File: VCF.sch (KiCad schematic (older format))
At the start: 70 parts, among them J101 AudioJack2, J102 AudioJack2, J103 AudioJack2, J104 AudioJack2, J105 Conn_02x05_Odd_Even, J106 AudioJack2, Q101 2N3906, Q102 2N3906, Q103 Q_NJFET_DSG, U101 TL072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

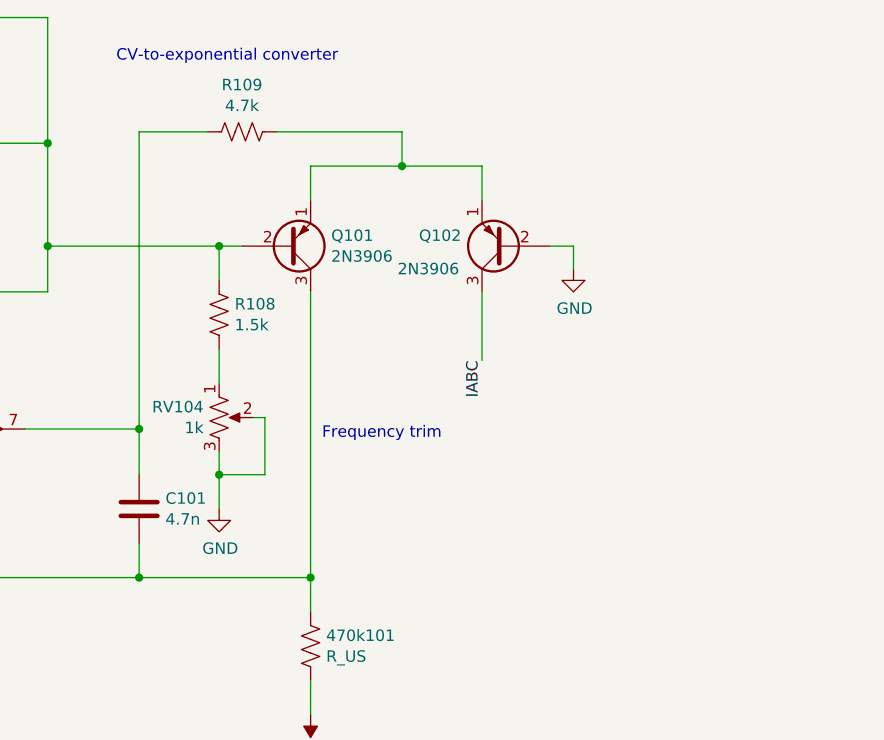
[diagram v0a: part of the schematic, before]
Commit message: Added SMT option for PNP current mirror
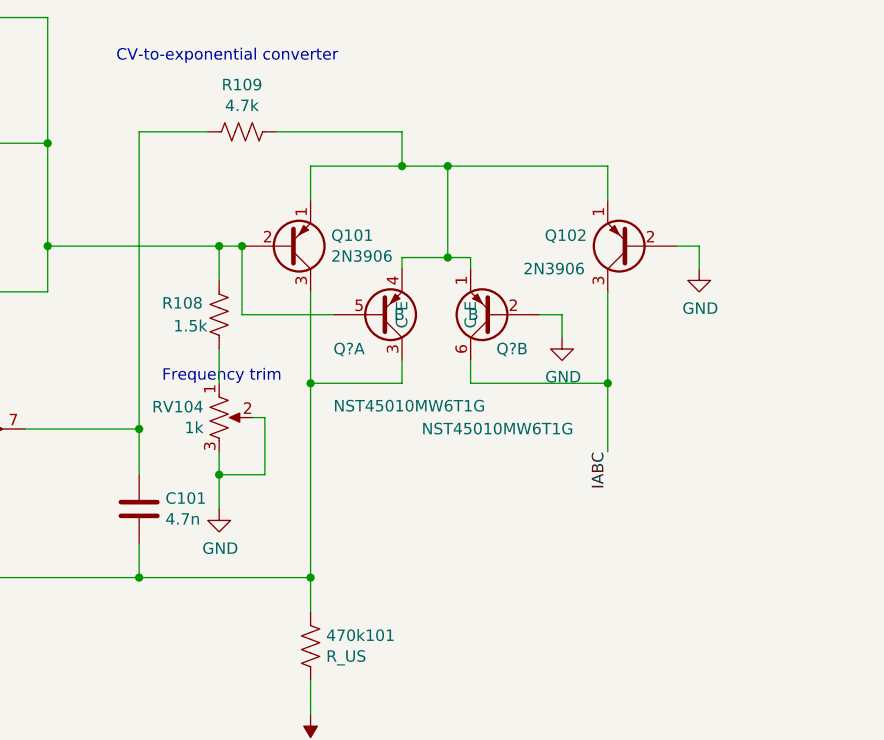
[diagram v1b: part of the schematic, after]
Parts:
- added Q? (x2): NST45010MW6T1G, symbol NST45010MW6T1G:NST45010MW6T1G
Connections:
- net GND: now also Q?.2 (B)
- net IABC: now also Q?.6 (C)
- net at 470k101.1, C101.2, Q101.3 (C)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: now also Q?.3 (C)
- net at Q101.2 (B), R101.1, R102.1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: now also Q?.5 (B)
- net at Q101.1 (E), Q102.1 (E), R109.1: now also Q?.1 (E), Q?.4 (E)
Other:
- moved on the sheet: Q102
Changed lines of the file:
@@
 U 1 1 60ABB8F0
 P 2900 5750
-F 0 "R108" H 2968 5796 50  0000 L CNN
-F 1 "1.5k" H 2968 5705 50  0000 L CNN
+F 0 "R108" H 2650 5800 50  0000 L CNN
+F 1 "1.5k" H 2700 5700 50  0000 L CNN
 F 2 "" V 2940 5740 50  0001 C CNN
 F 3 "~" H 2900 5750 50  0001 C CNN
@@
 	3300 5100 3700 5100
 Wire Wire Line
-	4050 5100 4050 5250
+	4600 5100 4600 5250
 Wire Wire Line
 	3150 4950 3700 4950
 Wire Wire Line
 	3700 4950 3700 5100
-Connection ~ 3700 5100
-Wire Wire Line
-	3700 5100 4050 5100
 Wire Wire Line
 	2550 4950 2550 6250
@@
 	2150 5450 2150 5650
 Wire Wire Line
-	4450 5550 4450 5450
-Wire Wire Line
-	4450 5450 4350 5450
+	5000 5550 5000 5450
+Wire Wire Line
+	5000 5450 4900 5450
 $Comp
 L power:GND #PWR0114
 U 1 1 60CA0F0A
-P 4450 5550
-F 0 "#PWR0114" H 4450 5300 50  0001 C CNN
-F 1 "GND" H 4455 5377 50  0000 C CNN
-F 2 "" H 4450 5550 50  0001 C CNN
-F 3 "" H 4450 5550 50  0001 C CNN
-	1    4450 5550
-	1    0    0    -1
-$EndComp
-Wire Wire Line
-	4050 5950 4050 5650
-Text Label 4050 5950 3    50   ~ 0
+P 5000 5550
+F 0 "#PWR0114" H 5000 5300 50  0001 C CNN
+F 1 "GND" H 5005 5377 50  0000 C CNN
+F 2 "" H 5000 5550 50  0001 C CNN
+F 3 "" H 5000 5550 50  0001 C CNN
+	1    5000 5550
+	1    0    0    -1
+$EndComp
+Text Label 4600 6350 3    50   ~ 0
 IABC
 $Comp
@@
 	1150 5900 1150 5800
 Wire Wire Line
-	3300 5650 3300 6900
+	3300 5650 3300 6050
 Wire Wire Line
 	2550 6900 3300 6900
@@
 Text Notes 9650 5150 0    50   ~ 0
 Power connector and decoupling
-Text Notes 3350 6300 0    50   ~ 0
+Text Notes 2650 6050 0    50   ~ 0
 Frequency trim
 $Comp
 L Transistor_BJT:2N3906 Q102
 U 1 1 61358B0B
-P 4150 5450
-F 0 "Q102" H 4341 5404 50  0000 L CNN
-F 1 "2N3906" H 4350 5550 50  0000 L CNN
-F 2 "Package_TO_SOT_THT:TO-92_Inline" H 4350 5375 50  0001 L CIN
-F 3 "https://www.onsemi.com/pub/Collateral/2N3906-D.PDF" H 4150 5450 50  0001 L CNN
-	1    4150 5450
+P 4700 5450
+F 0 "Q102" H 4891 5404 50  0000 L CNN
+F 1 "2N3906" H 4900 5550 50  0000 L CNN
+F 2 "Package_TO_SOT_THT:TO-92_Inline" H 4900 5375 50  0001 L CIN
+F 3 "https://www.onsemi.com/pub/Collateral/2N3906-D.PDF" H 4700 5450 50  0001 L CNN
+	1    4700 5450
 	-1   0    0    1
 $EndComp
@@
 NoConn ~ 6650 7450
 NoConn ~ 6250 7350
+$Comp
+L NST45010MW6T1G:NST45010MW6T1G Q?
+U 1 1 60A552FA
+P 3700 5250
+F 0 "Q?" H 3400 5900 50  0000 L CNN
+F 1 "NST45010MW6T1G" H 3400 6150 50  0000 L CNN
+F 2 "" H 3700 5250 50  0001 C CNN
+F 3 "" H 3700 5250 50  0001 C CNN
+	1    3700 5250
+	1    0    0    1
+$EndComp
+$Comp
+L NST45010MW6T1G:NST45010MW6T1G Q?
+U 2 1 60A57316
+P 4000 5250
+F 0 "Q?" H 3750 5900 50  0000 L CNN
+F 1 "NST45010MW6T1G" H 3550 6250 50  0000 L CNN
+F 2 "" H 4000 5250 50  0001 C CNN
+F 3 "" H 4000 5250 50  0001 C CNN
+	2    4000 5250
+	-1   0    0    1
+$EndComp
+Wire Wire Line
+	3700 5950 3700 6050
+Wire Wire Line
+	3700 6050 3300 6050
+Connection ~ 3300 6050
+Wire Wire Line
+	3300 6050 3300 6900
+Wire Wire Line
+	3700 5100 3900 5100
+Connection ~ 3700 5100
+Wire Wire Line
+	3700 5500 3700 5550
+Wire Wire Line
+	4000 5550 4000 5500
+Wire Wire Line
+	3700 5500 3900 5500
+Wire Wire Line
+	3900 5500 3900 5100
+Connection ~ 3900 5500
+Wire Wire Line
+	3900 5500 4000 5500
+Connection ~ 3900 5100
+Wire Wire Line
+	3900 5100 4600 5100
+Wire Wire Line
+	4600 6050 4000 6050
+Wire Wire Line
+	4000 6050 4000 5950
+Wire Wire Line
+	4600 5650 4600 6050
+Wire Wire Line
+	4600 6350 4600 6050
+Connection ~ 4600 6050
+Wire Wire Line
+	4400 5850 4400 5750
+Wire Wire Line
+	4400 5750 4300 5750
+$Comp
+L power:GND #PWR?
+U 1 1 60B3557E
+P 4400 5850
+F 0 "#PWR?" H 4400 5600 50  0001 C CNN
+F 1 "GND" H 4405 5677 50  0000 C CNN
+F 2 "" H 4400 5850 50  0001 C CNN
+F 3 "" H 4400 5850 50  0001 C CNN
+	1    4400 5850
+	1    0    0    -1
+$EndComp
+Wire Wire Line
+	3400 5750 3000 5750
+Wire Wire Line
+	3000 5750 3000 5450
+Connection ~ 3000 5450
 $EndSCHEMATC

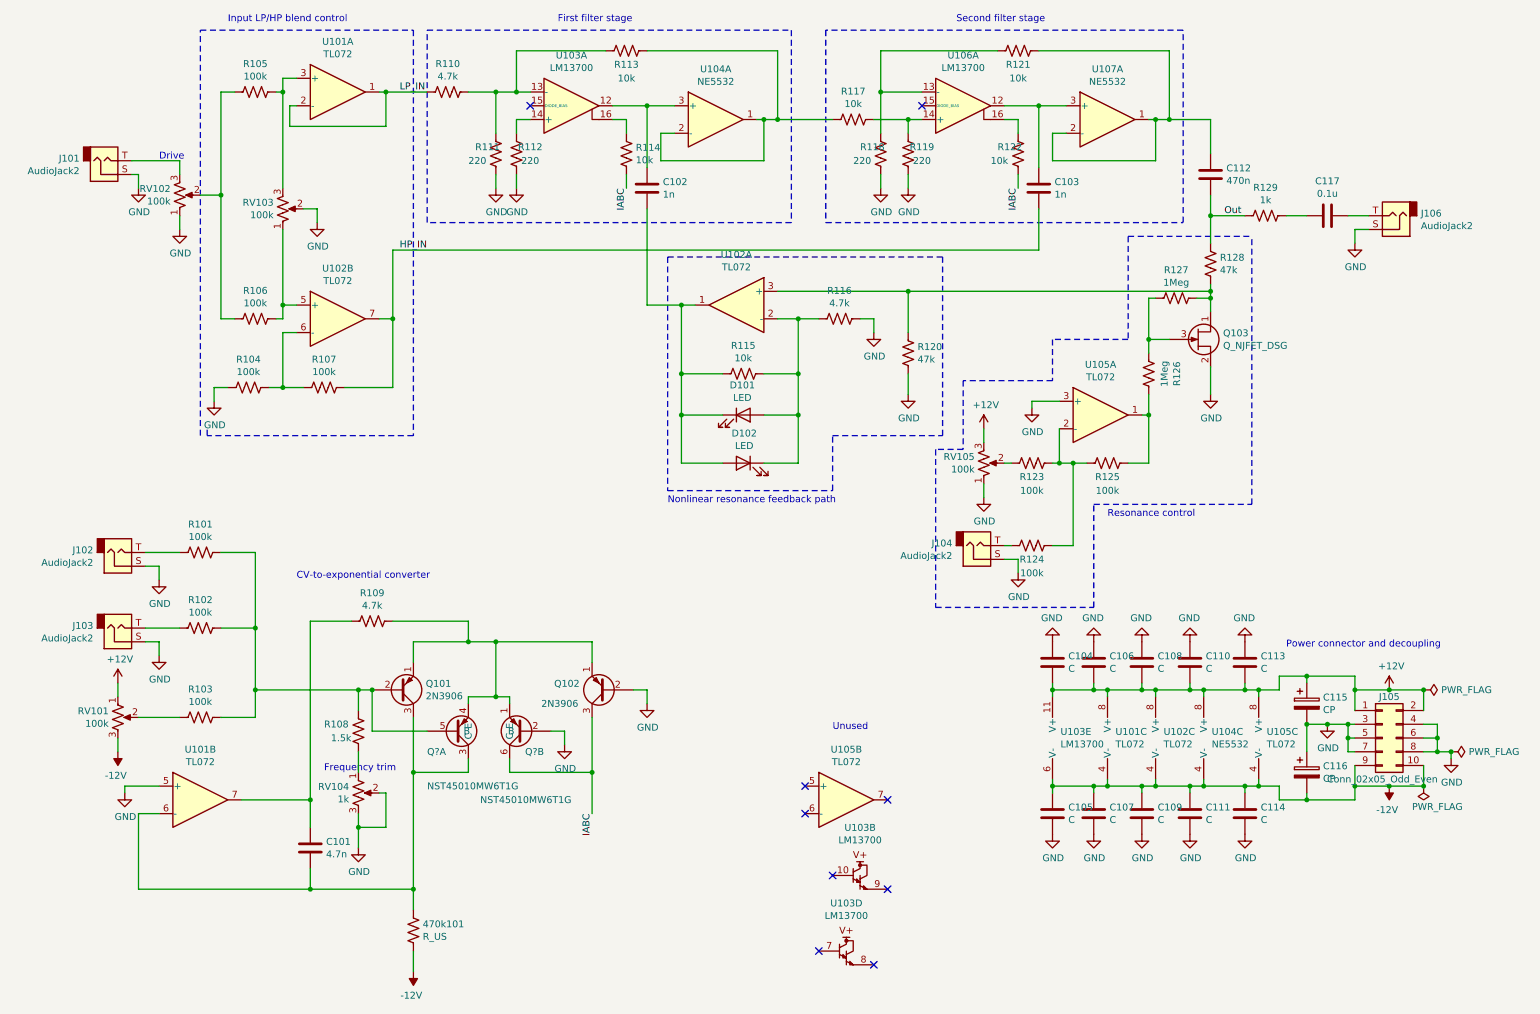
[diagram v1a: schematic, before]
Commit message: Assigned footprints to all components
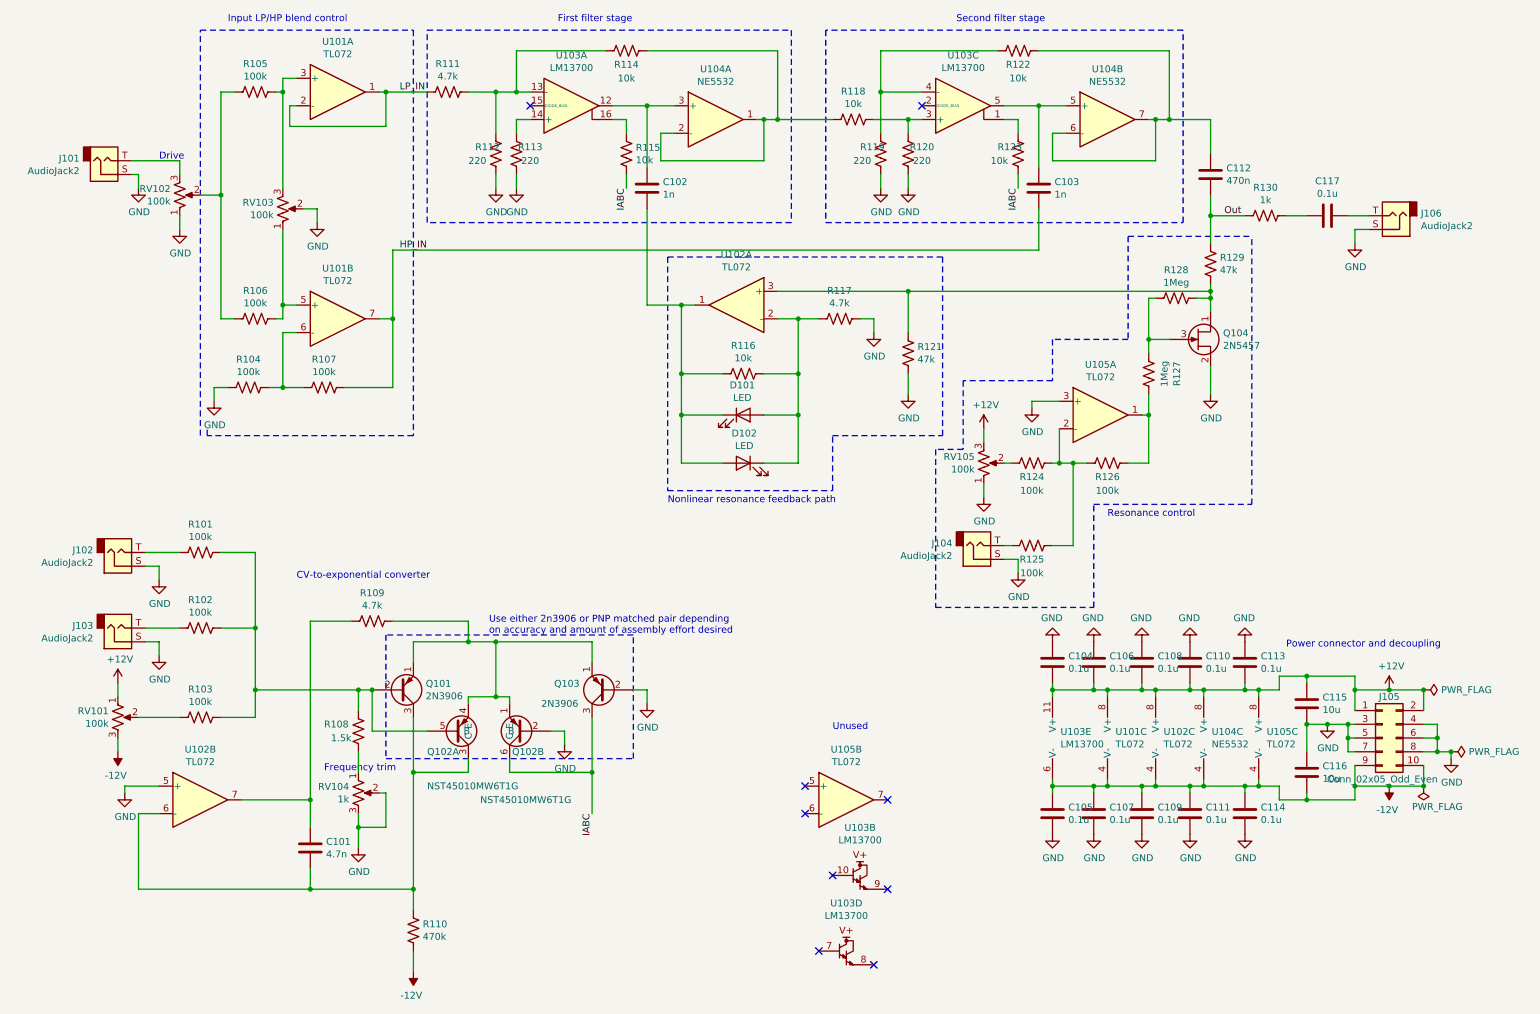
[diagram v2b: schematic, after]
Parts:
- removed C115, C116: CP, symbol Device:CP
- added C115, C116: 10u, Capacitor_SMD:C_0402_1005Metric, symbol Device:C
- C101: footprint (none) -> Capacitor_SMD:C_0402_1005Metric; LCSC (none) -> C1538
- C102, C103: footprint (none) -> Capacitor_SMD:C_0402_1005Metric; LCSC (none) -> C1523
- C104, C105, C106, C107, C108, C109, C110, C111, C113, C114: value C -> 0.1u; footprint (none) -> Capacitor_SMD:C_0402_1005Metric; LCSC (none) -> C1525
- C112: footprint (none) -> Capacitor_SMD:C_0402_1005Metric; LCSC (none) -> C47339
- C117: footprint (none) -> Capacitor_SMD:C_0402_1005Metric; LCSC (none) -> C1525
- D101, D102: footprint (none) -> LED_THT:LED_D5.0mm
- J101, J102, J103, J104, J106: footprint (none) -> A-5513:A-5513
- J105: footprint (none) -> Connector_PinHeader_2.54mm:PinHeader_2x05_P2.54mm_Vertical
- Q102: renamed from Q?; footprint (none) -> Package_TO_SOT_SMD:SOT-363_SC-70-6_Handsoldering
- Q104: renamed from Q103; value Q_NJFET_DSG -> 2N5457; footprint (none) -> Package_TO_SOT_THT:TO-92_Inline
- R101, R102, R103, R104, R105, R106, R107: footprint (none) -> Resistor_SMD:R_0402_1005Metric; LCSC (none) -> C25741
- R108: footprint (none) -> Resistor_SMD:R_0402_1005Metric; LCSC (none) -> C25867
- R109: footprint (none) -> Resistor_SMD:R_0402_1005Metric; LCSC (none) -> C25900
- R110: renamed from 470k101; value R_US -> 470k; footprint (none) -> Resistor_SMD:R_0402_1005Metric; LCSC (none) -> C25792
- R111: renamed from R110; footprint (none) -> Resistor_SMD:R_0402_1005Metric; LCSC (none) -> C25900
- R112: renamed from R111; footprint (none) -> Resistor_SMD:R_0402_1005Metric; LCSC (none) -> C25091
- R113: renamed from R112; footprint (none) -> Resistor_SMD:R_0402_1005Metric; LCSC (none) -> C25091
- R114: renamed from R113; footprint (none) -> Resistor_SMD:R_0402_1005Metric; LCSC (none) -> C25744
- R115: renamed from R114; footprint (none) -> Resistor_SMD:R_0402_1005Metric; LCSC (none) -> C25744
- R116: renamed from R115; footprint (none) -> Resistor_SMD:R_0402_1005Metric; LCSC (none) -> C25744
- R117: renamed from R116; footprint (none) -> Resistor_SMD:R_0402_1005Metric; LCSC (none) -> C25900
- R118: renamed from R117; footprint (none) -> Resistor_SMD:R_0402_1005Metric; LCSC (none) -> C25744
- R119: renamed from R118; footprint (none) -> Resistor_SMD:R_0402_1005Metric; LCSC (none) -> C25091
- R120: renamed from R119; footprint (none) -> Resistor_SMD:R_0402_1005Metric; LCSC (none) -> C25091
- R121: renamed from R120; footprint (none) -> Resistor_SMD:R_0402_1005Metric; LCSC (none) -> C25792
- R122: renamed from R121; footprint (none) -> Resistor_SMD:R_0402_1005Metric; LCSC (none) -> C25744
- R123: renamed from R122; footprint (none) -> Resistor_SMD:R_0402_1005Metric; LCSC (none) -> C25744
- R124: renamed from R123; footprint (none) -> Resistor_SMD:R_0402_1005Metric; LCSC (none) -> C25741
- R125: renamed from R124; footprint (none) -> Resistor_SMD:R_0402_1005Metric; LCSC (none) -> C25741
- R126: renamed from R125; footprint (none) -> Resistor_SMD:R_0402_1005Metric; LCSC (none) -> C25741
- R127: renamed from R126; footprint (none) -> Resistor_SMD:R_0402_1005Metric; LCSC (none) -> C26083
- R128: renamed from R127; footprint (none) -> Resistor_SMD:R_0402_1005Metric; LCSC (none) -> C26083
- R129: renamed from R128; footprint (none) -> Resistor_SMD:R_0402_1005Metric; LCSC (none) -> C25792
- R130: renamed from R129; footprint (none) -> Resistor_SMD:R_0402_1005Metric; LCSC (none) -> C11702
- RV101, RV102, RV103, RV105: footprint (none) -> A-2563:A-2563
- U101, U102, U105: footprint (none) -> Package_SO:SOIC-8_3.9x4.9mm_P1.27mm; LCSC (none) -> C6961
- U101: renamed from U102; footprint (none) -> Package_SO:SOIC-8_3.9x4.9mm_P1.27mm; LCSC (none) -> C6961
- U102: renamed from U101; footprint (none) -> Package_SO:SOIC-8_3.9x4.9mm_P1.27mm; LCSC (none) -> C6961
- U103: footprint (none) -> Package_DIP:DIP-16_W7.62mm
- U103: renamed from U106; footprint (none) -> Package_DIP:DIP-16_W7.62mm
- U104: footprint (none) -> Package_SO:SOIC-8_3.9x4.9mm_P1.27mm; LCSC (none) -> C7426
- U104: renamed from U107; footprint (none) -> Package_SO:SOIC-8_3.9x4.9mm_P1.27mm; LCSC (none) -> C7426
- renumbered Q102 to Q103
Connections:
- net +12V: now also C115.1
- net -12V: now also C116.2
- net GND: now also C115.2, C116.1
- net at C112.2, R122.1: now also U104.6 (-), U104.7; no longer U104.1, U104.2 (-)
- net at R119.1, R122.2: now also U103.4 (-); no longer U103.13 (-)
- net at R118.1, R120.1: now also U103.3 (+); no longer U103.14 (+)
- net at R123.1: now also U103.1; no longer U103.16
- new net: C103.1, U103.5, U104.5 (+)
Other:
- note added: "Use either 2n3906 or PNP matched pair depending \non accuracy and amount of assembly effort desired"

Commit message: Assigned footprints to all components
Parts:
- RV104: footprint (none) -> Potentiometer_THT:Potentiometer_Bourns_3296X_Horizontal
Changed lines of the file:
@@
 F 0 "RV104" H 2832 6246 50  0000 R CNN
 F 1 "1k" H 2832 6155 50  0000 R CNN
-F 2 "" H 2900 6200 50  0001 C CNN
+F 2 "Potentiometer_THT:Potentiometer_Bourns_3296X_Horizontal" H 2900 6200 50  0001 C CNN
 F 3 "~" H 2900 6200 50  0001 C CNN
 	1    2900 6200

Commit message: Assigned footprints to all components
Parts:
- J101, J102, J103, J104, J106: footprint A-5513:A-5513 -> A-2563:A-2563
- RV101, RV102, RV103, RV105: footprint A-2563:A-2563 -> A-5513:A-5513
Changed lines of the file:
@@
 F 0 "J101" H 871 1583 50  0000 R CNN
 F 1 "AudioJack2" H 871 1674 50  0000 R CNN
-F 2 "A-5513:A-5513" H 1050 1600 50  0001 C CNN
+F 2 "A-2563:A-2563" H 1050 1600 50  0001 C CNN
 F 3 "~" H 1050 1600 50  0001 C CNN
 	1    1050 1600
@@
 F 0 "J102" H 971 4433 50  0000 R CNN
 F 1 "AudioJack2" H 971 4524 50  0000 R CNN
-F 2 "A-5513:A-5513" H 1150 4450 50  0001 C CNN
+F 2 "A-2563:A-2563" H 1150 4450 50  0001 C CNN
 F 3 "~" H 1150 4450 50  0001 C CNN
 	1    1150 4450
@@
 F 0 "J103" H 971 4983 50  0000 R CNN
 F 1 "AudioJack2" H 971 5074 50  0000 R CNN
-F 2 "A-5513:A-5513" H 1150 5000 50  0001 C CNN
+F 2 "A-2563:A-2563" H 1150 5000 50  0001 C CNN
 F 3 "~" H 1150 5000 50  0001 C CNN
 	1    1150 5000
@@
 F 0 "J104" H 7221 4383 50  0000 R CNN
 F 1 "AudioJack2" H 7221 4474 50  0000 R CNN
-F 2 "A-5513:A-5513" H 7400 4400 50  0001 C CNN
+F 2 "A-2563:A-2563" H 7400 4400 50  0001 C CNN
 F 3 "~" H 7400 4400 50  0001 C CNN
 	1    7400 4400
@@
 F 0 "J106" H 10270 1983 50  0000 R CNN
 F 1 "AudioJack2" H 10270 2074 50  0000 R CNN
-F 2 "A-5513:A-5513" H 10450 2000 50  0001 C CNN
+F 2 "A-2563:A-2563" H 10450 2000 50  0001 C CNN
 F 3 "~" H 10450 2000 50  0001 C CNN
 	1    10450 2000
@@
 F 0 "RV102" H 1533 1804 50  0000 R CNN
 F 1 "100k" H 1533 1895 50  0000 R CNN
-F 2 "A-2563:A-2563" H 1600 1850 50  0001 C CNN
+F 2 "A-5513:A-5513" H 1600 1850 50  0001 C CNN
 F 3 "~" H 1600 1850 50  0001 C CNN
 	1    1600 1850
@@
 F 0 "RV103" H 2283 1904 50  0000 R CNN
 F 1 "100k" H 2283 1995 50  0000 R CNN
-F 2 "A-2563:A-2563" H 2350 1950 50  0001 C CNN
+F 2 "A-5513:A-5513" H 2350 1950 50  0001 C CNN
 F 3 "~" H 2350 1950 50  0001 C CNN
 	1    2350 1950
@@
 F 0 "RV101" H 1083 5696 50  0000 R CNN
 F 1 "100k" H 1083 5605 50  0000 R CNN
-F 2 "A-2563:A-2563" H 1150 5650 50  0001 C CNN
+F 2 "A-5513:A-5513" H 1150 5650 50  0001 C CNN
 F 3 "~" H 1150 5650 50  0001 C CNN
 	1    1150 5650
@@
 F 0 "RV105" H 7383 3754 50  0000 R CNN
 F 1 "100k" H 7383 3845 50  0000 R CNN
-F 2 "A-2563:A-2563" H 7450 3800 50  0001 C CNN
+F 2 "A-5513:A-5513" H 7450 3800 50  0001 C CNN
 F 3 "~" H 7450 3800 50  0001 C CNN
 	1    7450 3800

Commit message: fixed backwards cutoff frequency potentiometer
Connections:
- net +12V: now also RV101.3; no longer RV101.1
- net -12V: now also RV101.1; no longer RV101.3
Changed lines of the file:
@@
 F 3 "~" H 1150 5650 50  0001 C CNN
 	1    1150 5650
-	1    0    0    -1
+	1    0    0    1
 $EndComp
 Wire Wire Line
